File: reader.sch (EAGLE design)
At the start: 14 parts, among them J1 RJ11-6PTH

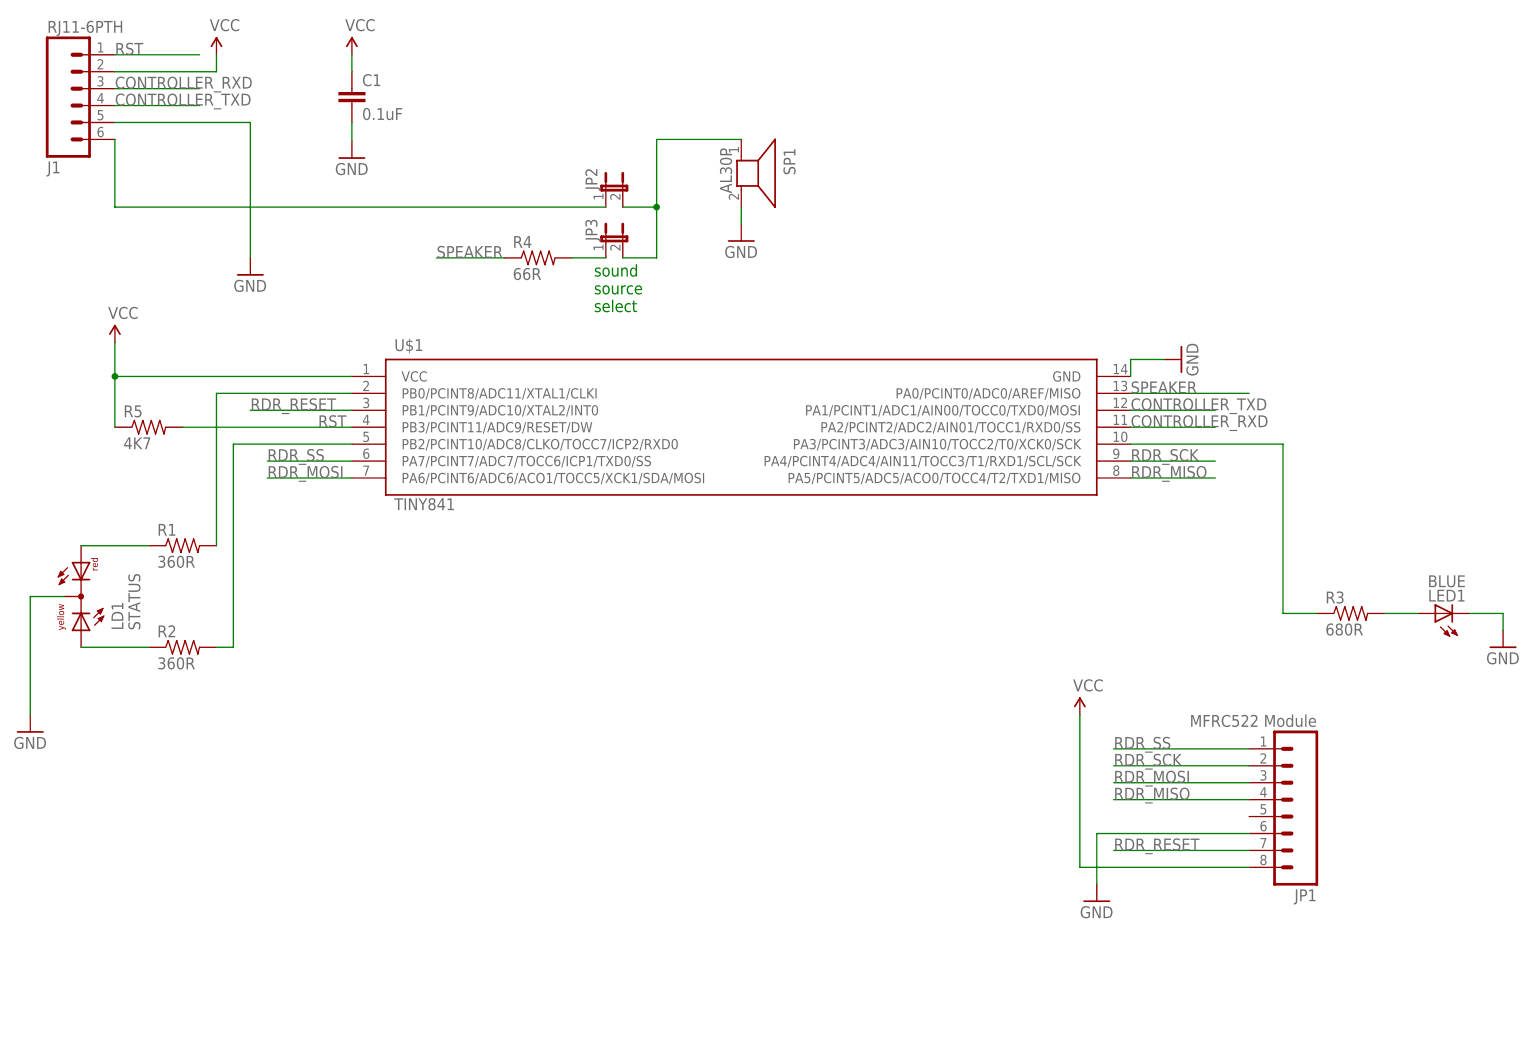
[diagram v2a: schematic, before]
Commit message: Add ISP header, minor layout modifications
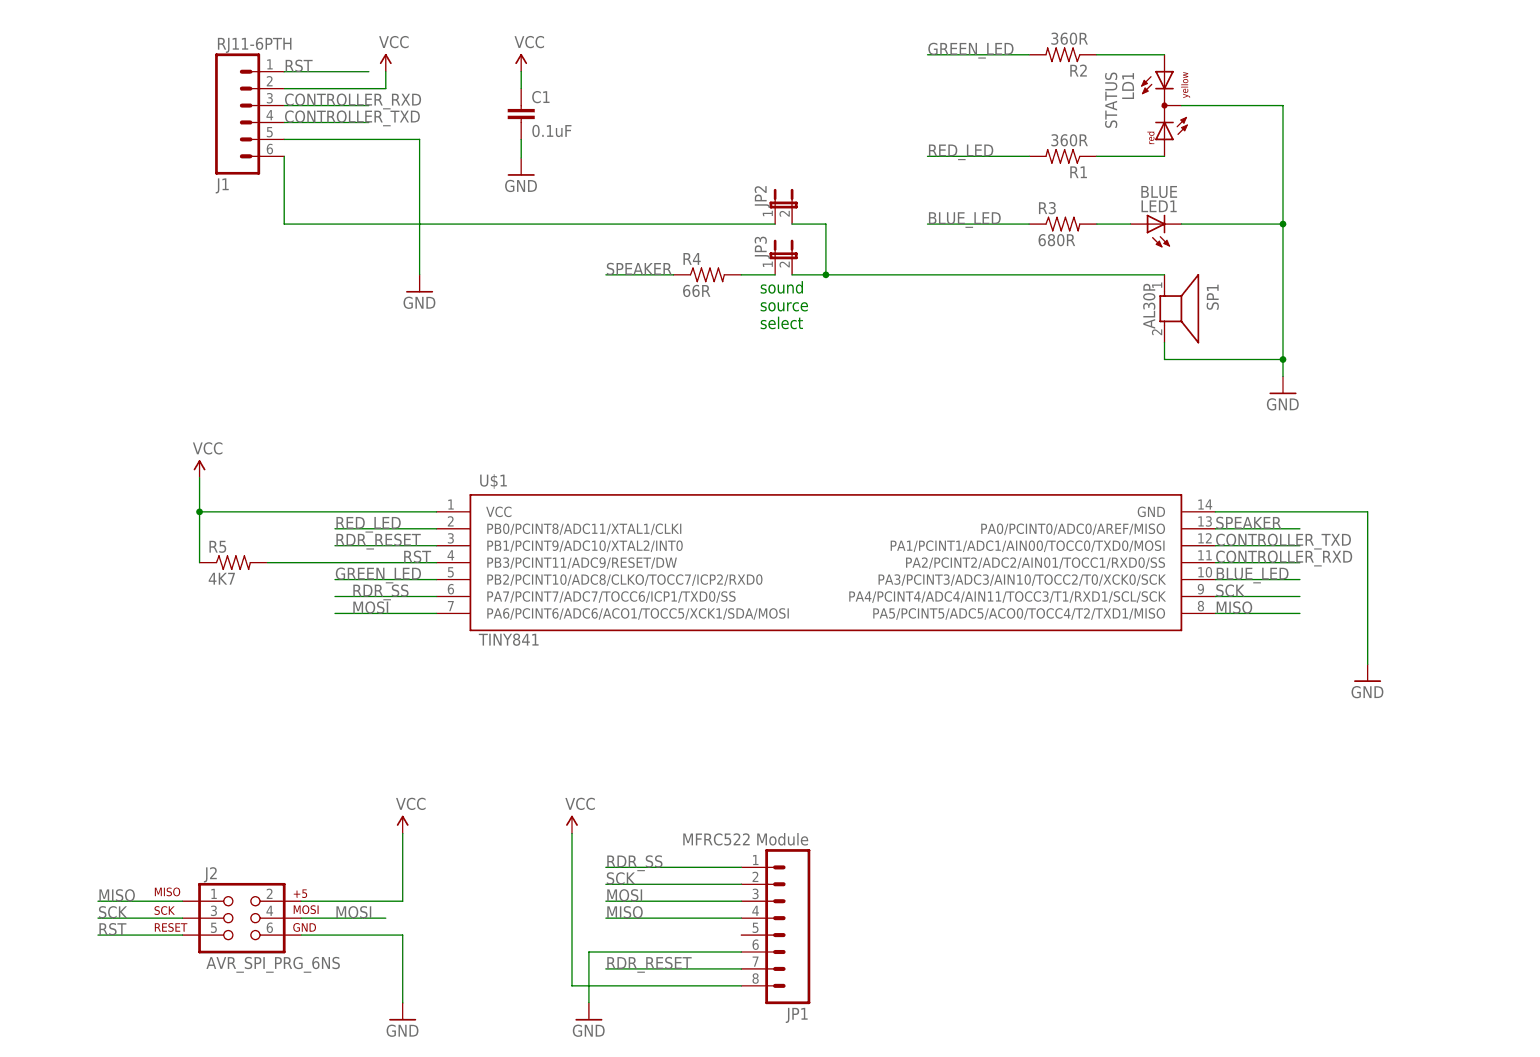
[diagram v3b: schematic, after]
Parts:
- added J2: AVR_SPI_PRG_6NS, SparkFun-Connectors:AVR_SPI_PRG_6NS
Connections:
- removed net RDR_MISO: JP1.4, U$1.PA5/PCINT5/ADC5/ACO0/TOCC4/T2/TXD1/MISO
- removed net RDR_MOSI: JP1.3, U$1.PA6/PCINT6/ADC6/ACO1/TOCC5/XCK1/SDA/MOSI
- removed net RDR_SCK: JP1.2, U$1.PA4/PCINT4/ADC4/AIN11/TOCC3/T1/RXD1/SCL/SCK
- new net MISO: J2.1, JP1.4, U$1.PA5/PCINT5/ADC5/ACO0/TOCC4/T2/TXD1/MISO
- new net MOSI: J2.4, JP1.3, U$1.PA6/PCINT6/ADC6/ACO1/TOCC5/XCK1/SDA/MOSI
- new net SCK: J2.3, JP1.2, U$1.PA4/PCINT4/ADC4/AIN11/TOCC3/T1/RXD1/SCL/SCK
- net GND: now also J2.6
- net RST: now also J2.5
- net VCC: now also J2.2
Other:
- moved on the sheet: C1, J1, JP1, JP2, JP3, LD1, LED1, R1, R2, R3, R4, R5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

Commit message: Change speaker footprint for the correct one
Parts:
- SP1: value AL30P -> AL23P; device buzzer:AL30P -> buzzer:AL23P
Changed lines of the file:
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@@
 <part name="LED1" library="led" deviceset="LED" device="3MM" value="BLUE"/>
 <part name="R3" library="SparkFun-Passives" deviceset="RESISTOR" device="0805-RES" value="680R"/>
-<part name="SP1" library="buzzer" deviceset="AL30P" device=""/>
 <part name="LD1" library="led" deviceset="DUOLED-RY-C" device="" value="STATUS"/>
 <part name="J1" library="SparkFun-Connectors" deviceset="RJ11-6" device="PTH"/>
@@
 <part name="SUPPLY5" library="SparkFun-Aesthetics" deviceset="VCC" device=""/>
 <part name="GND8" library="SparkFun-Aesthetics" deviceset="GND" device=""/>
+<part name="SP1" library="buzzer" deviceset="AL23P" device=""/>
 </parts>
 <sheets>
@@
 <instance part="LED1" gate="G$1" x="58.42" y="55.88" rot="R90"/>
 <instance part="R3" gate="G$1" x="45.72" y="55.88"/>
-<instance part="SP1" gate="G$1" x="60.96" y="43.18" rot="R270"/>
 <instance part="LD1" gate="G$1" x="60.96" y="73.66" rot="R180"/>
 <instance part="J1" gate="G$1" x="-76.2" y="73.66" rot="MR180"/>
@@
 <instance part="SUPPLY5" gate="G$1" x="-53.34" y="-35.56"/>
 <instance part="GND8" gate="1" x="-53.34" y="-63.5"/>
+<instance part="SP1" gate="G$1" x="60.96" y="43.18" rot="R270"/>
 </instances>
 <busses>
@@
 </segment>
 <segment>
-<pinref part="SP1" gate="G$1" pin="2"/>
 <wire x1="60.96" y1="35.56" x2="60.96" y2="38.1" width="0.1524" layer="91"/>
 <pinref part="GND3" gate="1" pin="GND"/>
@@
 <pinref part="LD1" gate="G$1" pin="C"/>
 <wire x1="78.74" y1="73.66" x2="63.5" y2="73.66" width="0.1524" layer="91"/>
+<pinref part="SP1" gate="G$1" pin="2"/>
 </segment>
 <segment>
@@
 <wire x1="5.08" y1="48.26" x2="10.16" y2="48.26" width="0.1524" layer="91"/>
 <wire x1="10.16" y1="48.26" x2="10.16" y2="55.88" width="0.1524" layer="91"/>
-<pinref part="SP1" gate="G$1" pin="1"/>
 <wire x1="60.96" y1="48.26" x2="10.16" y2="48.26" width="0.1524" layer="91"/>
 <junction x="10.16" y="48.26"/>
-</segment>
-</net>
+<pinref part="SP1" gate="G$1" pin="1"/>
+</segment>
+</net>

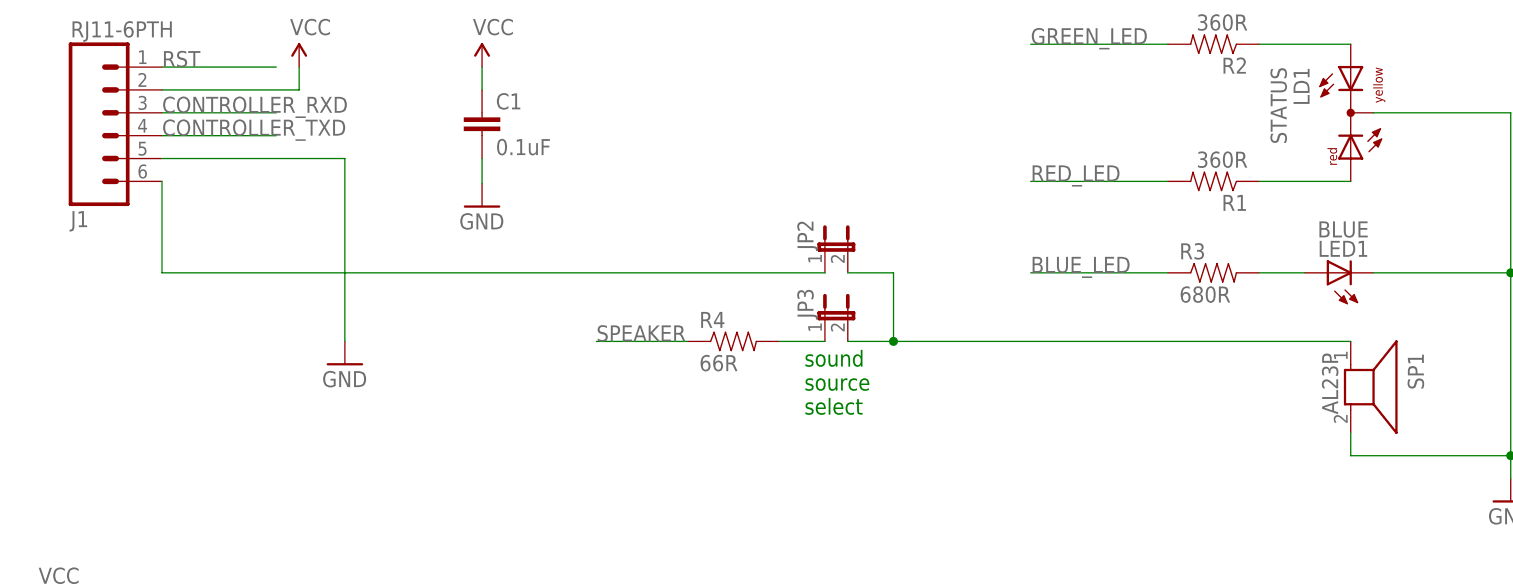
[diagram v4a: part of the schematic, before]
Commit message: Change sound source select jumpers to a single 3-pin jumper
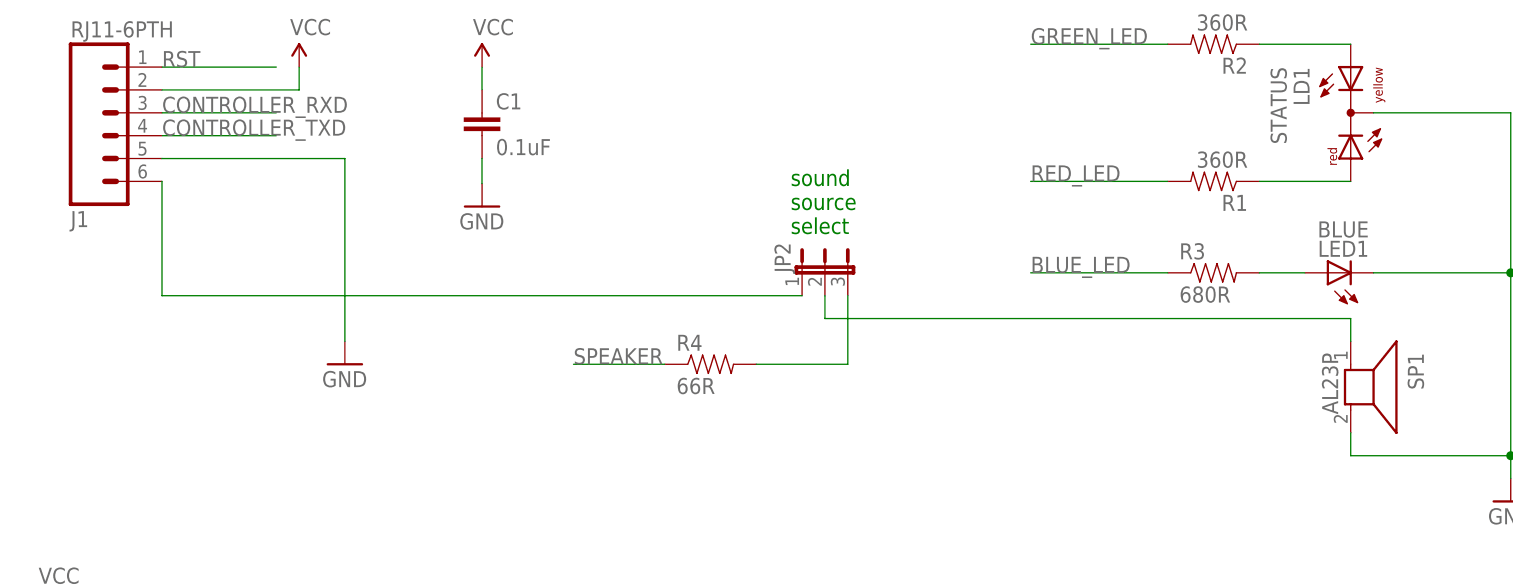
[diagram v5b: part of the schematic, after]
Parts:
- removed JP3: (no value), SparkFun-Retired:JUMPER-2PTH
- JP2: device SparkFun-Retired:JUMPER-2PTH -> jumper:JP2E
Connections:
- removed net N$4: JP2.2, JP3.2, SP1.1
- new net N$1: JP2.2, SP1.1
- net N$9: now also JP2.3; no longer JP3.1
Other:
- moved on the sheet: R4
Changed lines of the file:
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@@
 <part name="SUPPLY4" library="SparkFun-Aesthetics" deviceset="VCC" device=""/>
 <part name="R5" library="SparkFun-Passives" deviceset="RESISTOR" device="0805-RES" value="4K7"/>
-<part name="JP2" library="SparkFun-Retired" deviceset="JUMPER-2" device="PTH"/>
-<part name="JP3" library="SparkFun-Retired" deviceset="JUMPER-2" device="PTH"/>
 <part name="R4" library="SparkFun-Passives" deviceset="RESISTOR" device="0805-RES" value="66R"/>
 <part name="J2" library="SparkFun-Connectors" deviceset="AVR_SPI_PRG_6" device="NS"/>
@@
 <part name="GND8" library="SparkFun-Aesthetics" deviceset="GND" device=""/>
 <part name="SP1" library="buzzer" deviceset="AL23P" device=""/>
+<part name="JP2" library="jumper" deviceset="JP2E" device=""/>
 </parts>
 <sheets>
 <sheet>
 <plain>
-<text x="0.254" y="40.132" size="1.778" layer="91">sound
+<text x="-1.27" y="60.198" size="1.778" layer="91">sound
 source
 select</text>
@@
 <instance part="SUPPLY4" gate="G$1" x="-27.94" y="-35.56"/>
 <instance part="R5" gate="G$1" x="-78.74" y="5.08"/>
-<instance part="JP2" gate="A" x="2.54" y="58.42"/>
-<instance part="JP3" gate="A" x="2.54" y="50.8"/>
-<instance part="R4" gate="G$1" x="-7.62" y="48.26"/>
+<instance part="R4" gate="G$1" x="-10.16" y="45.72"/>
 <instance part="J2" gate="G$1" x="-78.74" y="-48.26"/>
 <instance part="SUPPLY5" gate="G$1" x="-53.34" y="-35.56"/>
 <instance part="GND8" gate="1" x="-53.34" y="-63.5"/>
 <instance part="SP1" gate="G$1" x="60.96" y="43.18" rot="R270"/>
+<instance part="JP2" gate="1" x="2.54" y="55.88"/>
 </instances>
 <busses>
@@
 <net name="EXT_SPEAKER" class="0">
 <segment>
-<pinref part="JP2" gate="A" pin="1"/>
 <pinref part="J1" gate="G$1" pin="6"/>
-<wire x1="2.54" y1="55.88" x2="-71.12" y2="55.88" width="0.1524" layer="91"/>
-<wire x1="-71.12" y1="55.88" x2="-71.12" y2="66.04" width="0.1524" layer="91"/>
+<wire x1="0" y1="53.34" x2="-71.12" y2="53.34" width="0.1524" layer="91"/>
+<wire x1="-71.12" y1="53.34" x2="-71.12" y2="66.04" width="0.1524" layer="91"/>
+<pinref part="JP2" gate="1" pin="1"/>
 </segment>
 </net>
@@
 <segment>
 <pinref part="R4" gate="G$1" pin="1"/>
-<wire x1="-12.7" y1="48.26" x2="-22.86" y2="48.26" width="0.1524" layer="91"/>
-<label x="-22.86" y="48.26" size="1.778" layer="95"/>
+<wire x1="-15.24" y1="45.72" x2="-25.4" y2="45.72" width="0.1524" layer="91"/>
+<label x="-25.4" y="45.72" size="1.778" layer="95"/>
 </segment>
 <segment>
@@
 <net name="N$9" class="0">
 <segment>
-<pinref part="JP3" gate="A" pin="1"/>
-<wire x1="2.54" y1="48.26" x2="-2.54" y2="48.26" width="0.1524" layer="91"/>
 <pinref part="R4" gate="G$1" pin="2"/>
-</segment>
-</net>
-<net name="N$4" class="0">
-<segment>
-<pinref part="JP2" gate="A" pin="2"/>
-<wire x1="5.08" y1="55.88" x2="10.16" y2="55.88" width="0.1524" layer="91"/>
-<pinref part="JP3" gate="A" pin="2"/>
-<wire x1="5.08" y1="48.26" x2="10.16" y2="48.26" width="0.1524" layer="91"/>
-<wire x1="10.16" y1="48.26" x2="10.16" y2="55.88" width="0.1524" layer="91"/>
-<wire x1="60.96" y1="48.26" x2="10.16" y2="48.26" width="0.1524" layer="91"/>
-<junction x="10.16" y="48.26"/>
+<wire x1="-5.08" y1="45.72" x2="5.08" y2="45.72" width="0.1524" layer="91"/>
+<wire x1="5.08" y1="45.72" x2="5.08" y2="53.34" width="0.1524" layer="91"/>
+<pinref part="JP2" gate="1" pin="3"/>
+</segment>
+</net>
+<net name="N$1" class="0">
+<segment>
+<wire x1="2.54" y1="53.34" x2="2.54" y2="50.8" width="0.1524" layer="91"/>
 <pinref part="SP1" gate="G$1" pin="1"/>
-</segment>
-</net>
+<wire x1="2.54" y1="50.8" x2="60.96" y2="50.8" width="0.1524" layer="91"/>
+<wire x1="60.96" y1="50.8" x2="60.96" y2="48.26" width="0.1524" layer="91"/>
+<pinref part="JP2" gate="1" pin="2"/>
+</segment>
+</net>
